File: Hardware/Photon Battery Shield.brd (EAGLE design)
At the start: 40.6 x 35.6 mm, 24 parts, among them U1 MAX1704X, U2 MCP73831

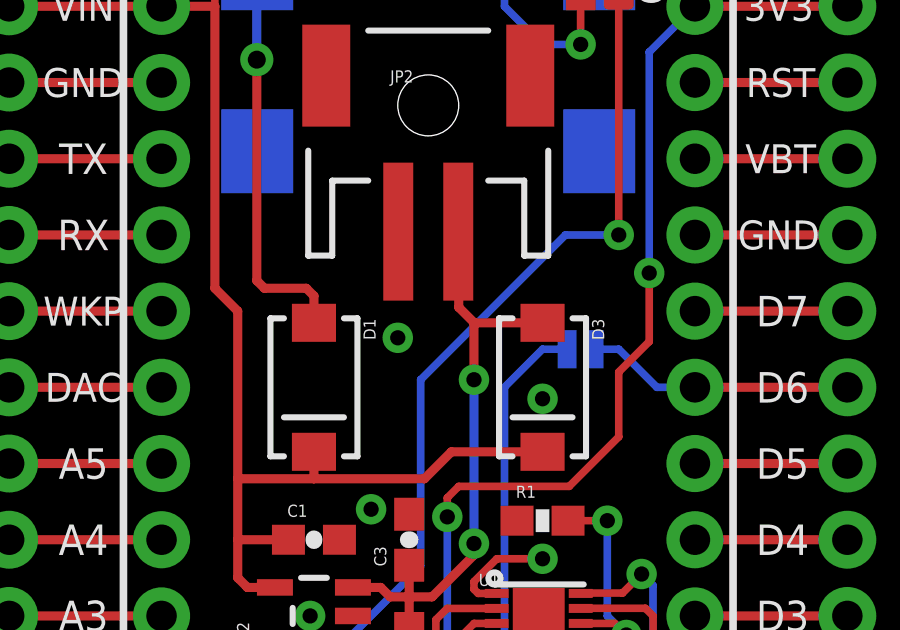
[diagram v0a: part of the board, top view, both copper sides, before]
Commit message: Adding test point to VBAT. Reducing bSilk on barrel jack to avoid going over board.
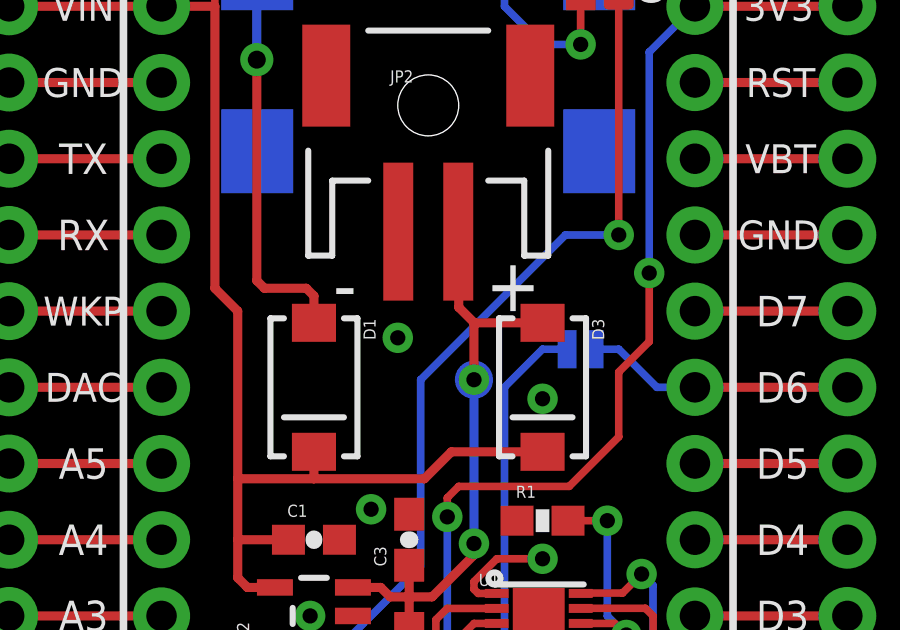
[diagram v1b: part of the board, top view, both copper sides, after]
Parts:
- added TP1: TEST-POINT3X5, SparkFun-Passives:PAD.03X.05
- JP1: value DNP -> 5.5x2.1mm Barrel
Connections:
- net VBAT: now also TP1.P$1
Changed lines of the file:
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@@
 <layer number="27" name="tValues" color="7" fill="1" visible="no" active="yes"/>
 <layer number="28" name="bValues" color="7" fill="1" visible="no" active="yes"/>
-<layer number="29" name="tStop" color="7" fill="3" visible="yes" active="yes"/>
+<layer number="29" name="tStop" color="7" fill="3" visible="no" active="yes"/>
 <layer number="30" name="bStop" color="7" fill="6" visible="no" active="yes"/>
 <layer number="31" name="tCream" color="7" fill="4" visible="no" active="yes"/>
@@
 <layer number="47" name="Measures" color="7" fill="1" visible="no" active="yes"/>
 <layer number="48" name="Document" color="7" fill="1" visible="no" active="yes"/>
-<layer number="49" name="Reference" color="7" fill="1" visible="no" active="yes"/>
+<layer number="49" name="Reference" color="7" fill="1" visible="yes" active="yes"/>
 <layer number="50" name="dxf" color="7" fill="1" visible="no" active="no"/>
 <layer number="51" name="tDocu" color="6" fill="1" visible="yes" active="yes"/>
@@
 </element>
 <element name="JP2" library="SparkFun-Connectors" package="JST-2-SMD" value="" x="20.32" y="27.94">
-<attribute name="PROD_ID" value="CONN-08352" x="20.32" y="27.94" size="1.778" layer="27" display="off"/>
+<attribute name="PROD_ID" value="CONN-11443" x="20.32" y="27.94" size="1.778" layer="27" display="off"/>
 </element>
 <element name="JP3" library="template_temp" package="SPARK_PHOTON_TEMPLATE_WIDE" value="SPARK_PHOTONTEMPLATE_WIDE" x="10.16" y="0"/>
@@
 <attribute name="PROD_ID" value="IC-10399" x="24.003" y="11.43" size="1.778" layer="27" display="off"/>
 </element>
-<element name="JP1" library="SparkFun-Connectors" package="POWER_JACK_SMD" value="DNP" x="20.32" y="33.02" rot="MR270">
+<element name="JP1" library="SparkFun-Connectors" package="POWER_JACK_SMD" value="5.5x2.1mm Barrel" x="20.32" y="33.02" rot="MR270">
 <attribute name="PROD_ID" value="CONN-08106" x="20.32" y="33.02" size="1.778" layer="28" rot="MR270" display="off"/>
 <attribute name="VALUE" value="5.5x2.1mm Barrel" x="20.32" y="33.02" size="1.778" layer="28" rot="MR270" display="off"/>
+<attribute name="SF_ID" value="PRT-12748" x="20.32" y="33.02" size="1.778" layer="28" rot="MR270" display="off"/>
 </element>
 <element name="D1" library="SparkFun-DiscreteSemi" package="SMA-DIODE" value="MBRA140" x="16.51" y="19.05" rot="R270">
@@
 <element name="LOGO3" library="SparkFun-Aesthetics" package="SFE_LOGO_NAME_FLAME_.1" value="SFE_LOGO_NAME_FLAME.1_INCH" x="5.588" y="10.795" rot="R90"/>
 <element name="SJ1" library="SparkFun-Passives" package="PAD-JUMPER-2-NO_YES_SILK" value="alert" x="25.4" y="20.32" rot="MR0"/>
+<element name="TP1" library="SparkFun-Passives" package="PAD.03X.05" value="TEST-POINT3X5" x="21.844" y="19.304" rot="MR0"/>
 </elements>
 <signals>
@@
 <wire x1="20.447" y1="12.065" x2="21.844" y2="13.462" width="0.3048" layer="1"/>
 <wire x1="21.844" y1="13.462" x2="21.844" y2="13.843" width="0.3048" layer="1"/>
+<contactref element="TP1" pad="P$1"/>
 </signal>
 <signal name="N$5">
